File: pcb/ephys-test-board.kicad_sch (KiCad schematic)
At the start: 1 part, among them J5 Conn_02x10_Odd_Even

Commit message: Remove battery power option
- This device needs user IO
- Battery power means there would need to be a touch screen or wireless
  connection. Too complex.
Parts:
- J5: footprint (none) -> Connector_PinSocket_2.54mm:PinSocket_2x10_P2.54mm_Vertical

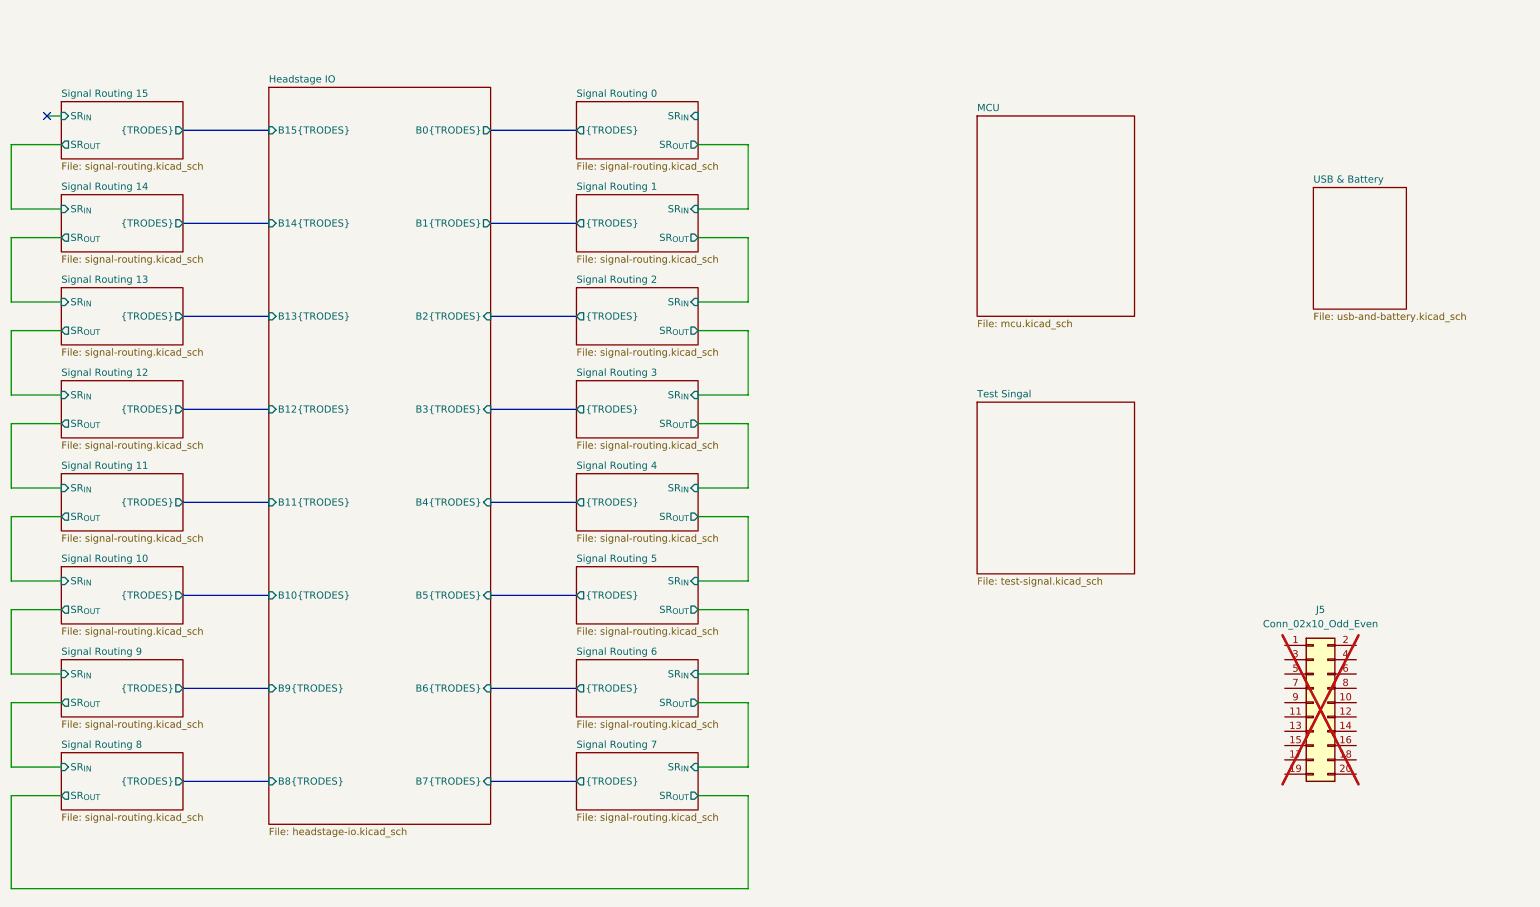
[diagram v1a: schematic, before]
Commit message: Finished schematic, started routing
- There is a 8-channel motif that will need to be copied 16x on the
  board. I'm not sure the most efficient way to do this.
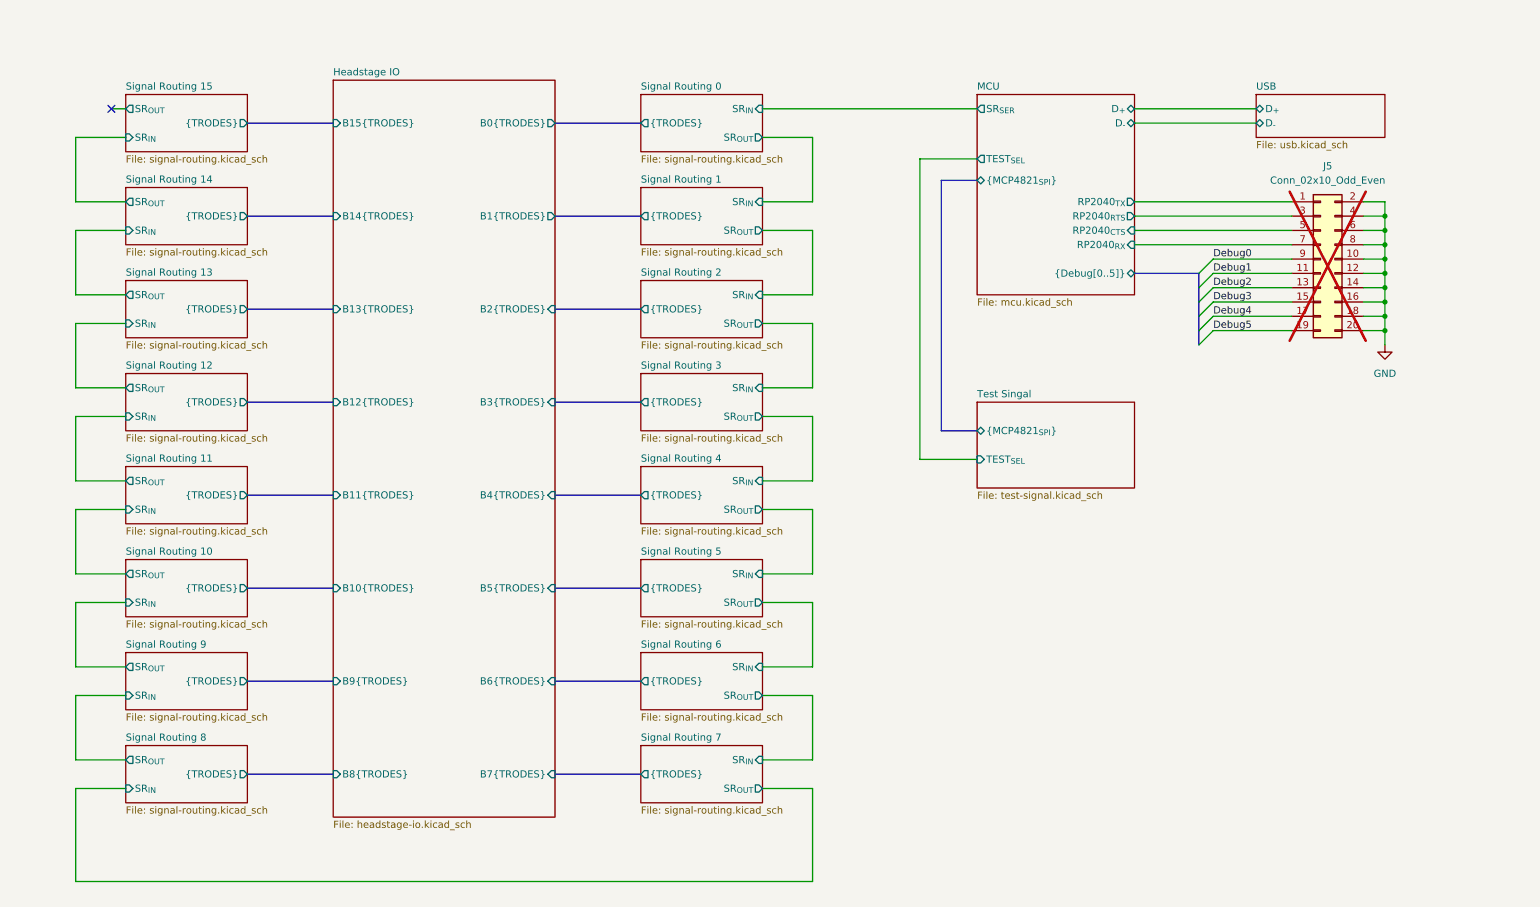
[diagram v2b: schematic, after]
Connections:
- net MCU/RP2040_{TX}: now reaches J5.1 (Pin_1)
- net GND: now reaches J5.10 (Pin_10)
- net GND: now also J5.12 (Pin_12), J5.14 (Pin_14), J5.16 (Pin_16), J5.18 (Pin_18), J5.2 (Pin_2), J5.20 (Pin_20), J5.4 (Pin_4), J5.6 (Pin_6), J5.8 (Pin_8)
- net Debug1: now reaches J5.11 (Pin_11)
- net Debug2: now reaches J5.13 (Pin_13)
- net Debug3: now reaches J5.15 (Pin_15)
- net Debug4: now reaches J5.17 (Pin_17)
- net Debug5: now reaches J5.19 (Pin_19)
- net MCU/RP2040_{RTS}: now reaches J5.3 (Pin_3)
- net MCU/RP2040_{CTS}: now reaches J5.5 (Pin_5)
- net MCU/RP2040_{RX}: now reaches J5.7 (Pin_7)
- net Debug0: now reaches J5.9 (Pin_9)
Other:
- sheet USB & Battery renamed USB
- sheet MCU ports: added D_{+}, D_{-}, RP2040_{CTS}, RP2040_{RTS}, RP2040_{RX}, RP2040_{TX}, SR_{SER}, TEST_{SEL}, {Debug[0..5]}, {MCP4821_{SPI}}; removed none
- sheet Test Singal ports: added TEST_{SEL}, {MCP4821_{SPI}}; removed none
- sheet USB: file usb-and-battery.kicad_sch -> usb.kicad_sch
- sheet USB ports: added D_{+}, D_{-}; removed none
- moved on the sheet: J5

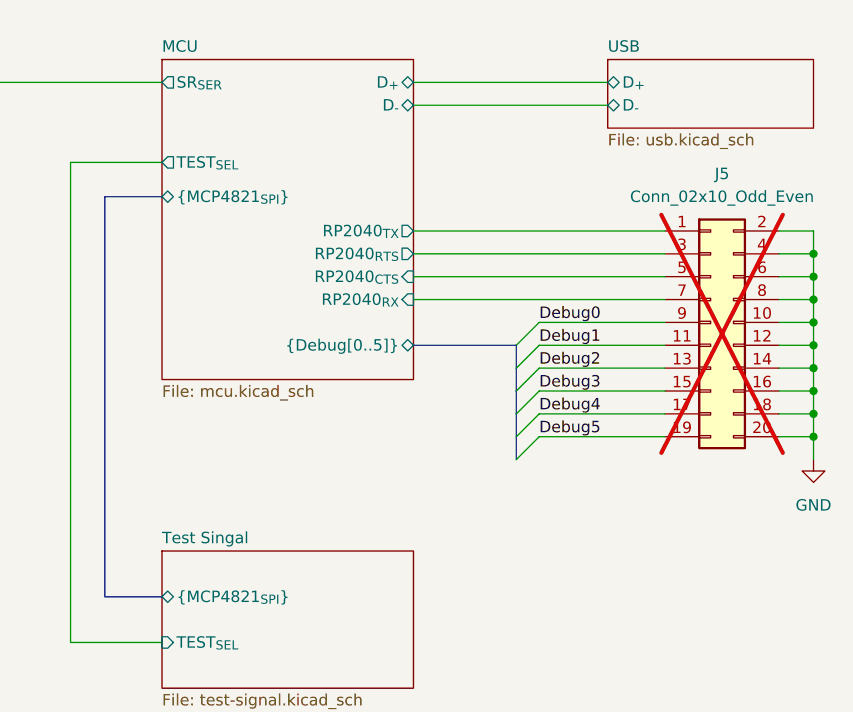
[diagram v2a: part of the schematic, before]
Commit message: Motif is repeated
- some components are grouped by function
- components are roughly organized within groups
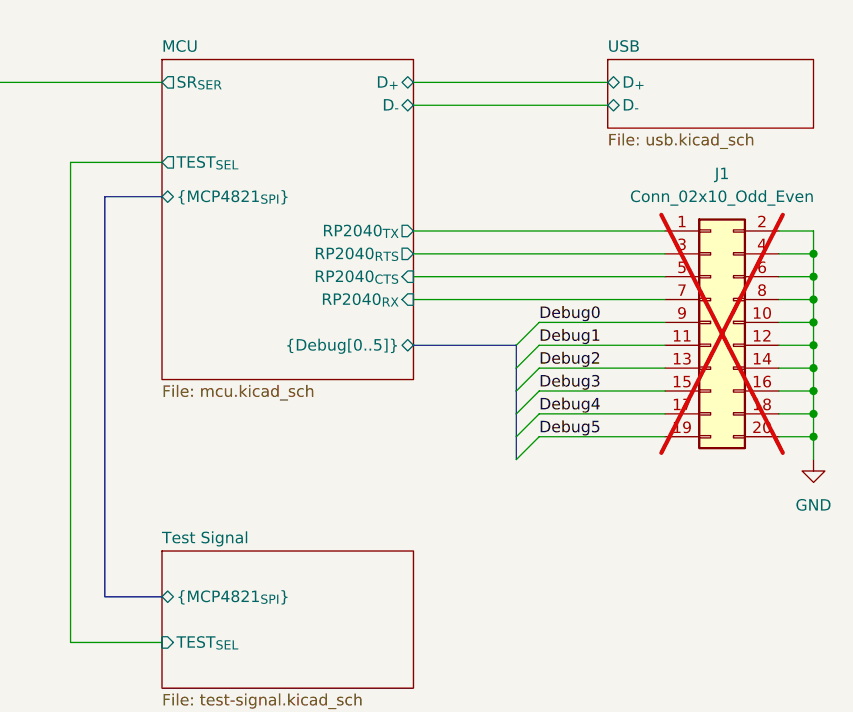
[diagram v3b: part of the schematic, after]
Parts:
- renumbered J5 to J1
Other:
- sheet Test Singal renamed Test Signal
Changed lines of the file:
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@@
 		(dnp no)
 		(fields_autoplaced yes)
-		(property "Reference" "#PWR0608"
+		(property "Reference" "#PWR01"
 			(at 261.62 86.36 0)
 			(effects
@@
 			(project "ephys-test-board"
 				(path "/ffaa6ffd-73fa-4da3-9ff1-78fa7369281f"
-					(reference "#PWR0608")
+					(reference "#PWR01")
 					(unit 1)
 				)
@@
 		(dnp yes)
 		(fields_autoplaced yes)
-		(property "Reference" "J5"
+		(property "Reference" "J1"
 			(at 251.46 48.26 0)
 			(effects
@@
 			(project "ephys-test-board"
 				(path "/ffaa6ffd-73fa-4da3-9ff1-78fa7369281f"
-					(reference "J5")
+					(reference "J1")
 					(unit 1)
 				)
@@
 			(color 0 0 0 0.0000)
 		)
-		(property "Sheetname" "Test Singal"
+		(property "Sheetname" "Test Signal"
 			(at 189.23 89.4584 0)
 			(effects

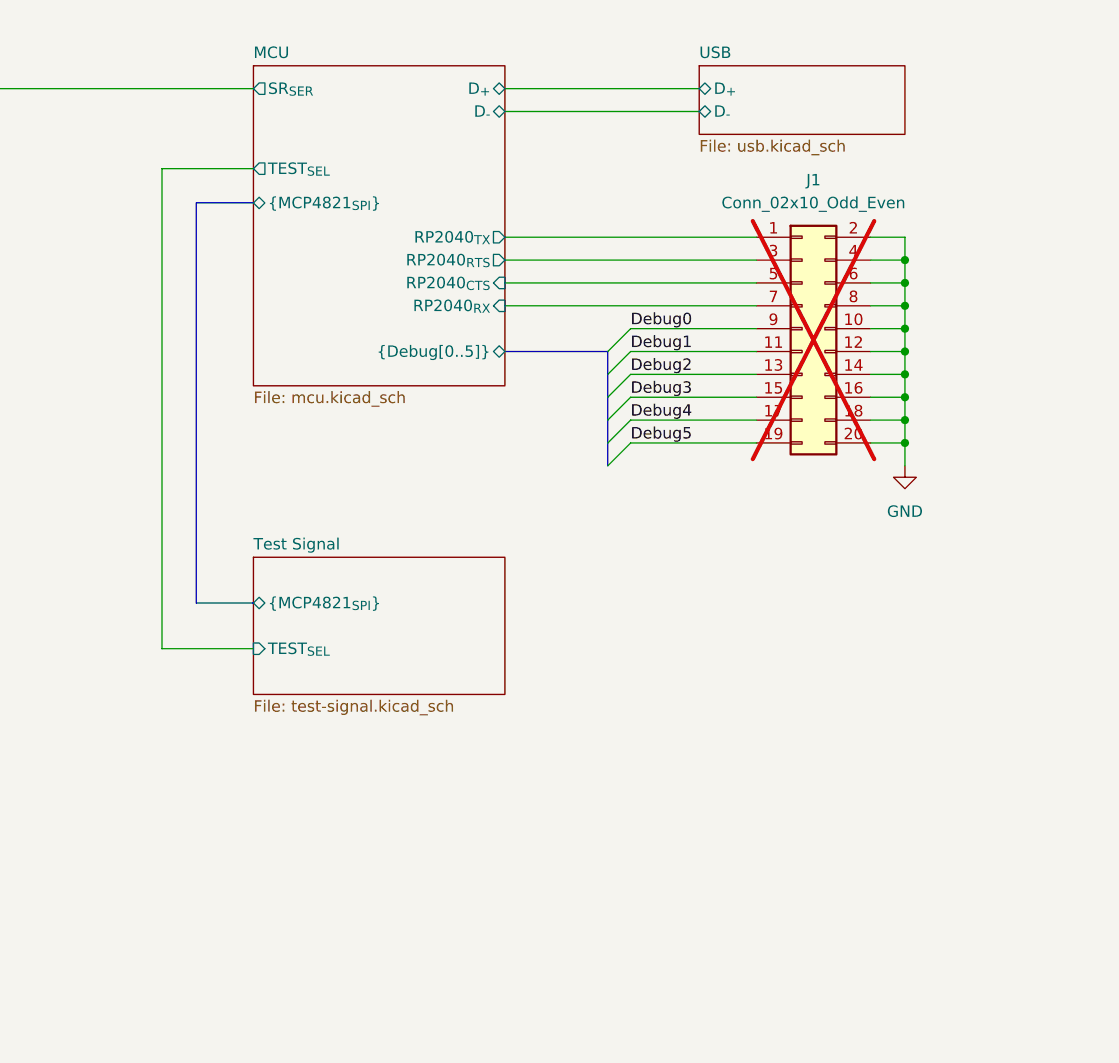
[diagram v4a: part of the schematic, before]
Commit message: Added user IO and battery
- Battery provides noise free operation
- OLED display and rotary encoder are not that hard to use
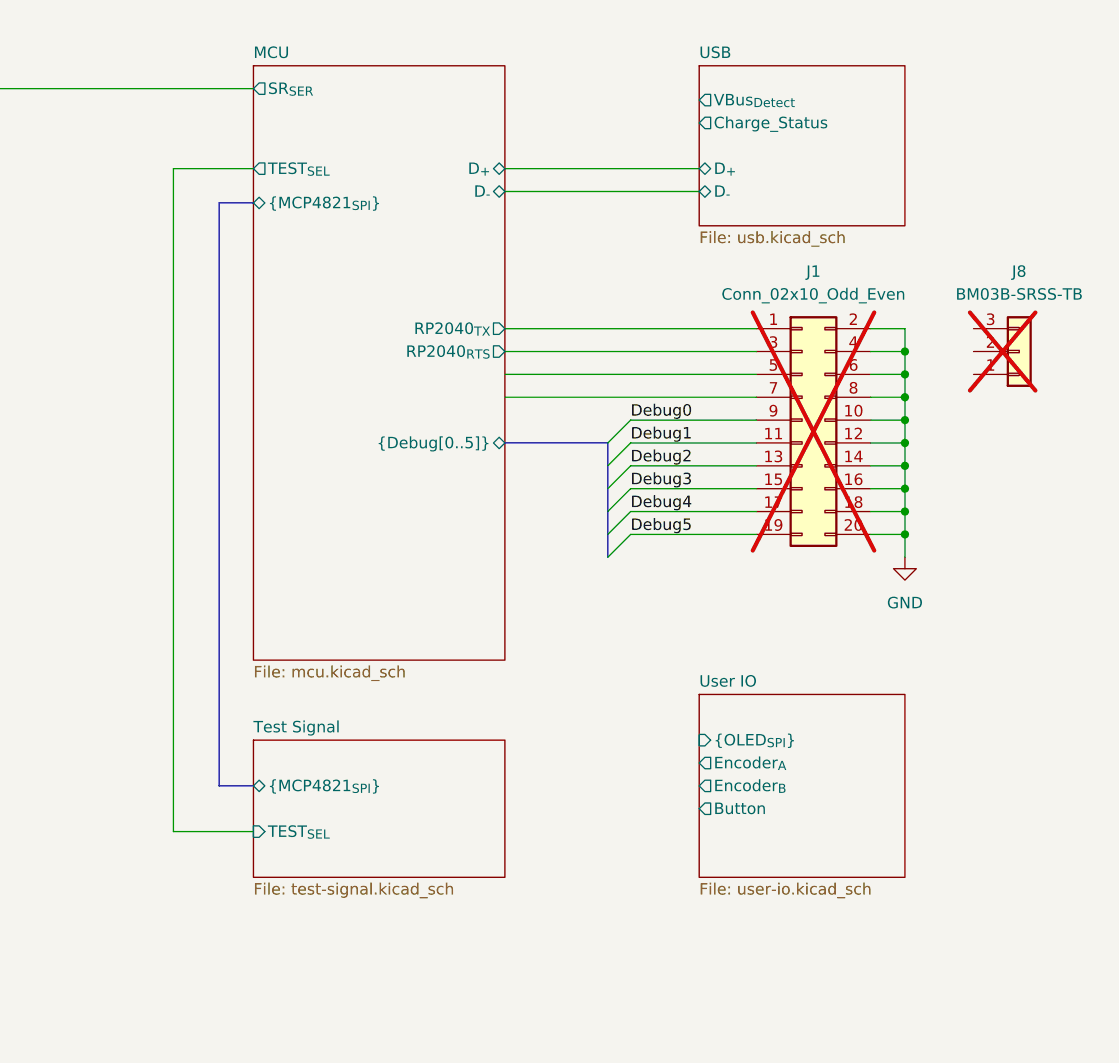
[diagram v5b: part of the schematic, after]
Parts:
- added J8: BM03B-SRSS-TB, Connector_JST:JST_SH_BM03B-SRSS-TB_1x03-1MP_P1.00mm_Vertical, symbol Connector_Generic:Conn_01x03
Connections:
- net MCU/RP2040_{CTS}: no longer names the net of J1.5 (Pin_5)
- net MCU/RP2040_{RX}: no longer names the net of J1.7 (Pin_7)
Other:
- added sheet User IO (user-io.kicad_sch)
- sheet MCU ports: added none; removed RP2040_{CTS}, RP2040_{RX}
- sheet USB ports: added Charge_Status, VBus_{Detect}; removed none
- moved on the sheet: J1

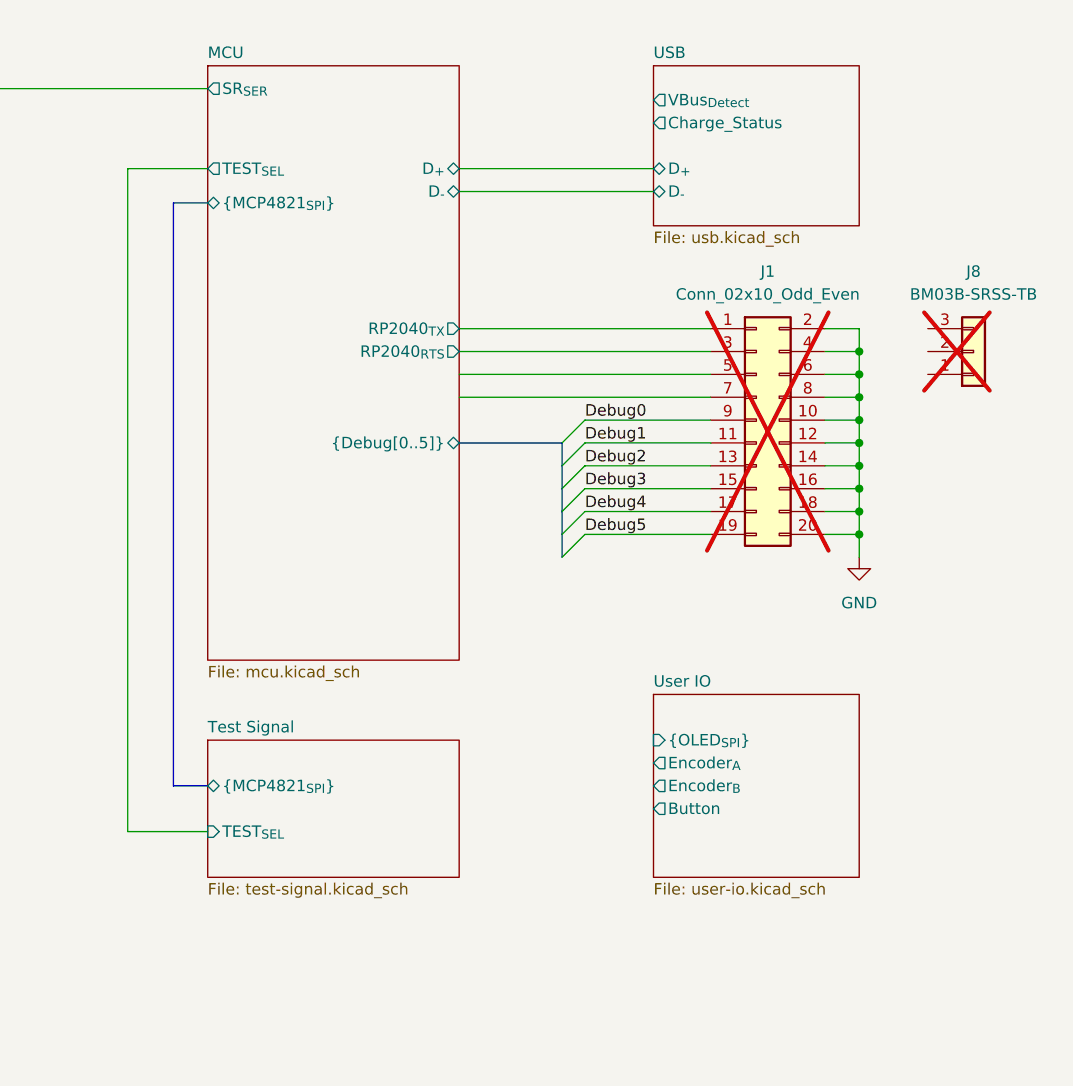
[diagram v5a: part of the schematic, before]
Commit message: Initial Rev. A schematic
- I think this has everything we need for revision A
- Battery charge indication via the OLED display
- User interface via rotary encoder/select switch
- Cycle through affected individual channels, none, or all
- Cycle through amplitudes
- Cycle through frequencies
- Select signal source
- Cycle through pre-loaded channel maps?
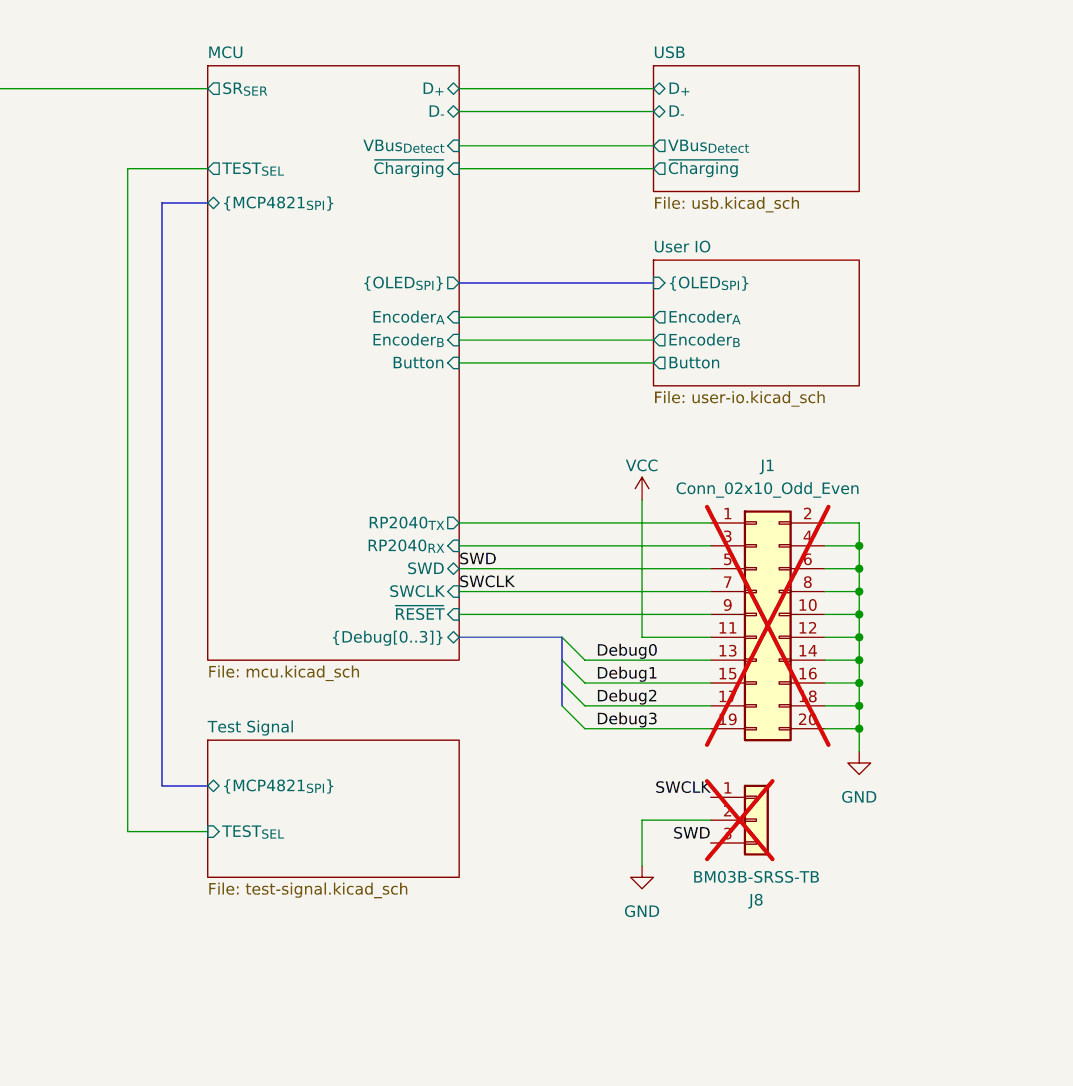
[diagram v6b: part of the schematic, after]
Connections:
- net Debug4 is gone; now on net Debug2: J1.17 (Pin_17)
- net Debug5 is gone; now on net Debug3: J1.19 (Pin_19)
- net Debug0: now also J1.13 (Pin_13); no longer J1.9 (Pin_9)
- net Debug1: now also J1.15 (Pin_15); no longer J1.11 (Pin_11)
- net Debug2: no longer J1.13 (Pin_13)
- net Debug3: no longer J1.15 (Pin_15)
- net GND: now also J8.2 (Pin_2)
- net SWD: now reaches J1.5 (Pin_5)
- net SWD: now also J8.3 (Pin_3)
- net SWCLK: now reaches J1.7 (Pin_7)
- net SWCLK: now also J8.1 (Pin_1)
- net MCU/RP2040_{RTS} renamed MCU/RP2040_{RX}
- new net MCU/~{RESET}: J1.9 (Pin_9)
- new net VCC: J1.11 (Pin_11)
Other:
- sheet MCU ports: added Button, Encoder_{A}, Encoder_{B}, RP2040_{RX}, SWCLK, SWD, VBus_{Detect}, {Debug[0..3]}, {OLED_{SPI}}, ~{Charging}, ~{RESET}; removed RP2040_{RTS}, {Debug[0..5]}
- sheet USB ports: added ~{Charging}; removed Charge_Status
- moved on the sheet: J1, J8
